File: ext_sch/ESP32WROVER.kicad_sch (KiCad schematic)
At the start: 4 parts, among them U4 ESP32-WROVER

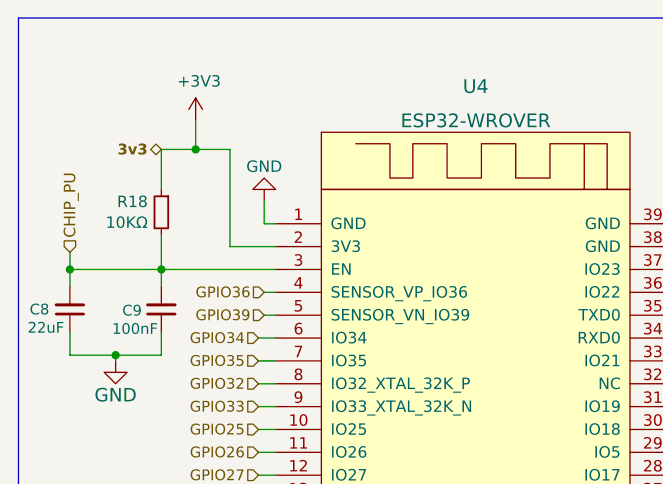
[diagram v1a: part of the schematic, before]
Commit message: Latest revision: 3v3 LDO replaced with buck converter, 5v0 buck replaced, LED configuration changed, speaker terminals replaced with sping connector, and new audio pepriheral FPC connector added. Besides this all data traces have been rerouted, the board has been shortened about 8mm.
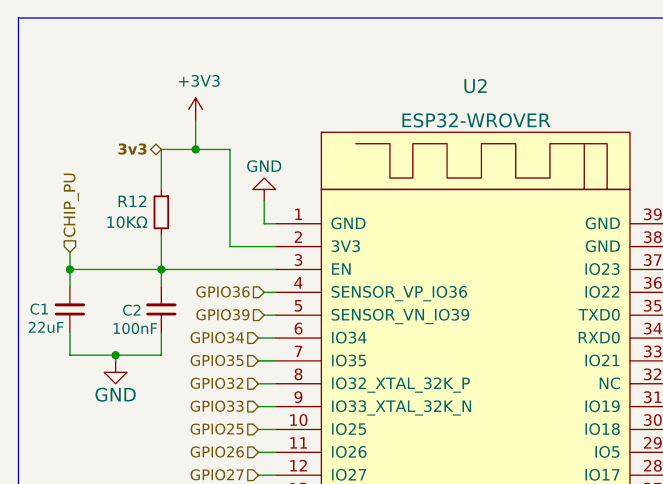
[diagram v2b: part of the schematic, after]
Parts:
- renumbered C8 to C1, C9 to C2, R18 to R12, U4 to U2
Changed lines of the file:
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@@
   (symbol (lib_id "power:GND") (at 24.765 52.07 0) (unit 1)
     (in_bom yes) (on_board yes)
-    (property "Reference" "#SUPPLY04" (id 0) (at 24.765 52.07 0)
+    (property "Reference" "#SUPPLY05" (id 0) (at 24.765 52.07 0)
       (effects (font (size 1.27 1.27)) hide)
     )
@@
   (symbol (lib_id "Device:C_Small") (at 29.845 46.355 180) (unit 1)
     (in_bom yes) (on_board yes)
-    (property "Reference" "C9" (id 0) (at 27.686 46.482 0)
+    (property "Reference" "C2" (id 0) (at 27.686 46.482 0)
       (effects (font (size 1.1938 1.1938)) (justify left))
     )
@@
   (symbol (lib_id "power:+3V3") (at 33.655 25.4 0) (unit 1)
     (in_bom yes) (on_board yes)
-    (property "Reference" "#PWR049" (id 0) (at 33.655 29.21 0)
+    (property "Reference" "#PWR045" (id 0) (at 33.655 29.21 0)
       (effects (font (size 1.27 1.27)) hide)
     )
@@
   (symbol (lib_id "power:GND") (at 41.275 34.29 180) (unit 1)
     (in_bom yes) (on_board yes)
-    (property "Reference" "#PWR051" (id 0) (at 41.275 27.94 0)
+    (property "Reference" "#PWR047" (id 0) (at 41.275 27.94 0)
       (effects (font (size 1.27 1.27)) hide)
     )
@@
   (symbol (lib_id "power:GND") (at 40.005 72.39 270) (unit 1)
     (in_bom yes) (on_board yes)
-    (property "Reference" "#PWR050" (id 0) (at 33.655 72.39 0)
+    (property "Reference" "#PWR046" (id 0) (at 33.655 72.39 0)
       (effects (font (size 1.27 1.27)) hide)
     )
@@
   (symbol (lib_id "power:GND") (at 91.44 38.1 90) (unit 1)
     (in_bom yes) (on_board yes)
-    (property "Reference" "#PWR052" (id 0) (at 97.79 38.1 0)
+    (property "Reference" "#PWR048" (id 0) (at 97.79 38.1 0)
       (effects (font (size 1.27 1.27)) hide)
     )
@@
   (symbol (lib_id "Device:R_Small") (at 29.845 35.56 0) (mirror y) (unit 1)
     (in_bom yes) (on_board yes)
-    (property "Reference" "R18" (id 0) (at 28.3464 34.3916 0)
+    (property "Reference" "R12" (id 0) (at 28.3464 34.3916 0)
       (effects (font (size 1.27 1.27)) (justify left))
     )
@@
   (symbol (lib_id "Device:C_Small") (at 19.685 46.355 180) (unit 1)
     (in_bom yes) (on_board yes)
-    (property "Reference" "C8" (id 0) (at 17.399 46.355 0)
+    (property "Reference" "C1" (id 0) (at 17.399 46.355 0)
       (effects (font (size 1.1938 1.1938)) (justify left))
     )
@@
   (symbol (lib_id "Lib:ESP32-WROVER") (at 65.405 55.88 0) (unit 1)
     (in_bom yes) (on_board yes) (fields_autoplaced)
-    (property "Reference" "U4" (id 0) (at 64.77 21.59 0)
+    (property "Reference" "U2" (id 0) (at 64.77 21.59 0)
       (effects (font (size 1.524 1.524)))
     )
